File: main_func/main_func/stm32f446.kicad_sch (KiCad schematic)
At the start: 14 parts, among them J10 Conn_01x01_Male, J9 Conn_01x06_Male, SW2 SW_Push, U7 STM32F446RETx, Y1 8MHz

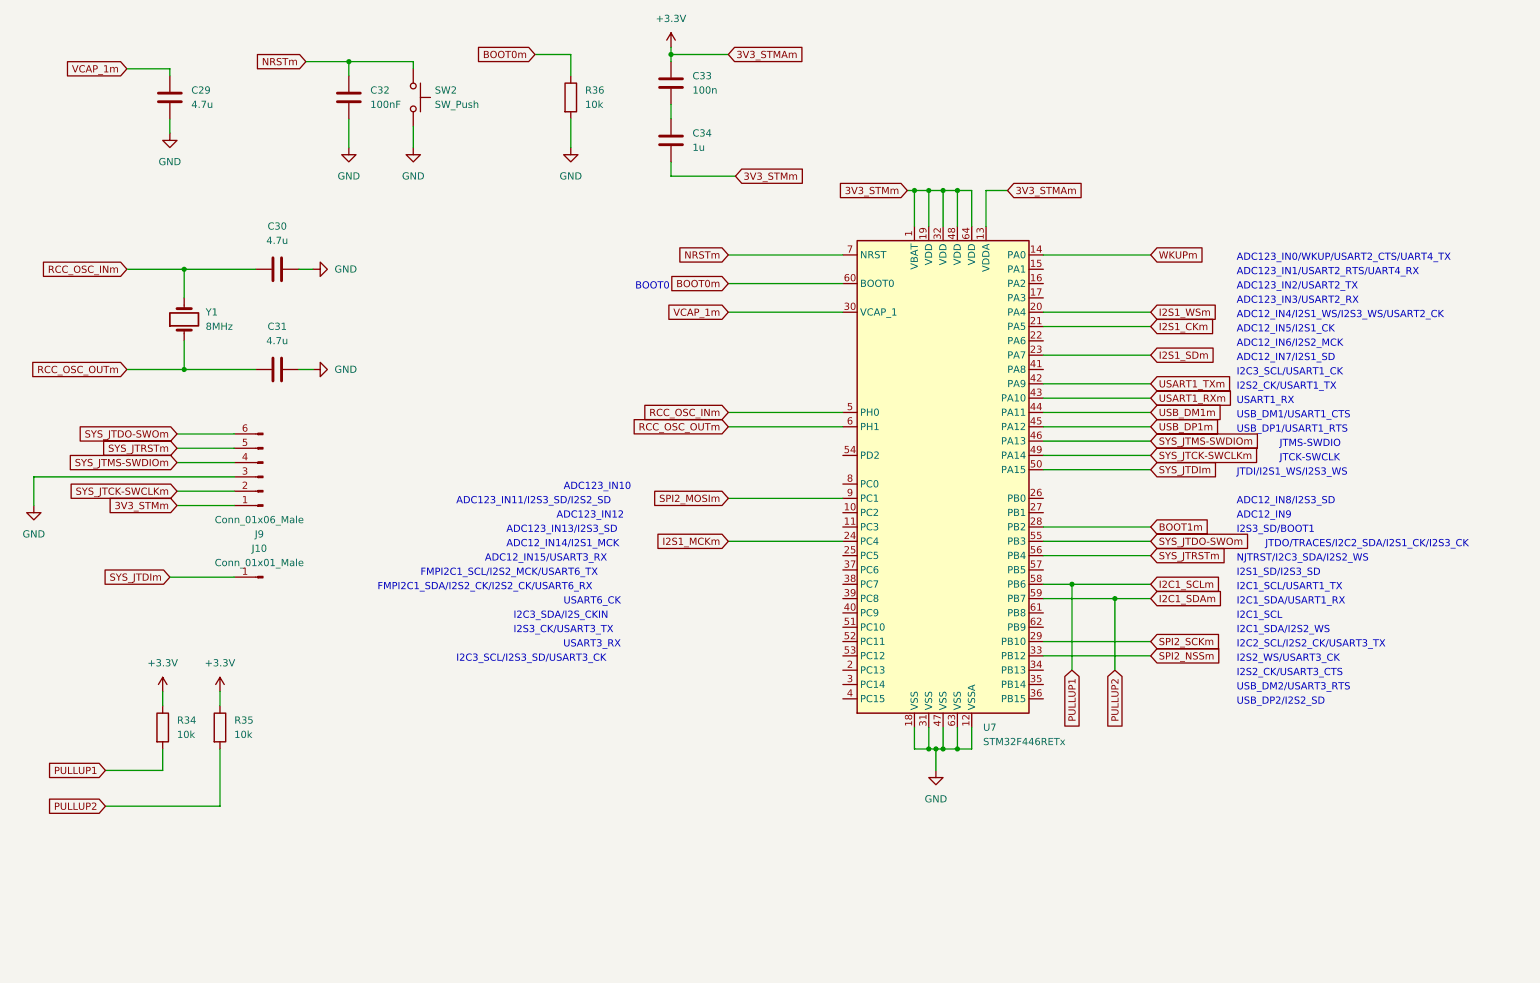
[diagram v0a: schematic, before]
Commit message: main func schematics fixed
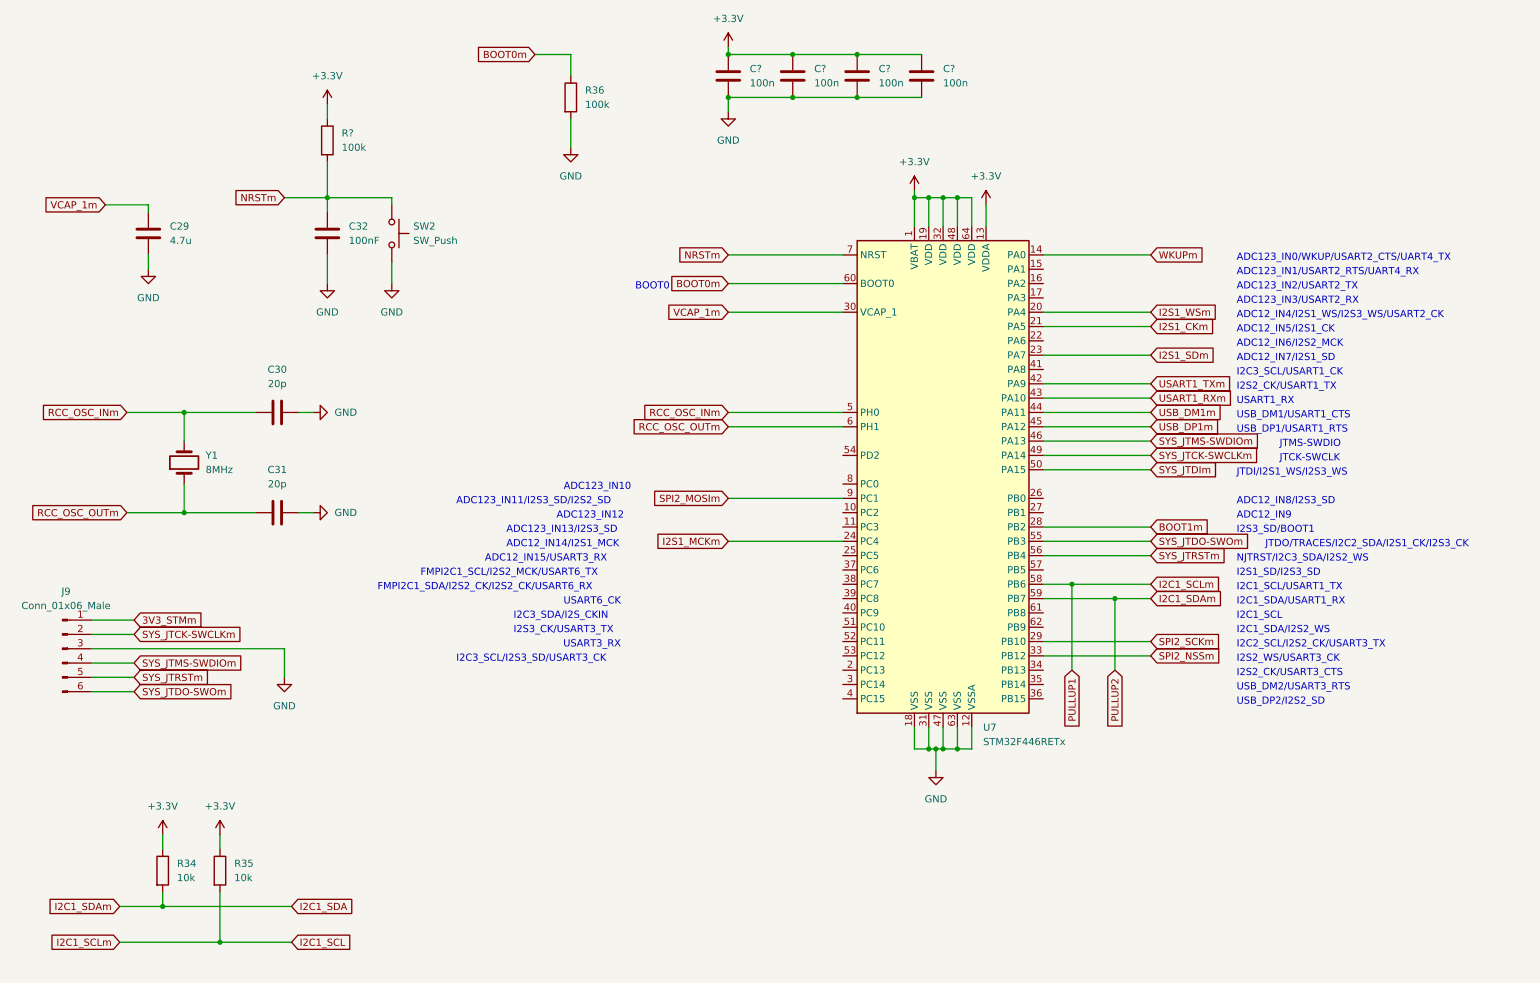
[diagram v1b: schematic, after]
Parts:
- removed C33: 100n, Capacitor_SMD:C_0805_2012Metric_Pad1.18x1.45mm_HandSolder, symbol Device:C
- removed C34: 1u, Capacitor_SMD:C_0805_2012Metric_Pad1.18x1.45mm_HandSolder, symbol Device:C
- removed J10: Conn_01x01_Male, Connector_PinSocket_2.54mm:PinSocket_1x01_P2.54mm_Horizontal, symbol Connector:Conn_01x01_Male
- added C? (x4): 100n, Capacitor_SMD:C_0805_2012Metric_Pad1.18x1.45mm_HandSolder, symbol Device:C
- added R?: 100k, Resistor_SMD:R_0805_2012Metric_Pad1.20x1.40mm_HandSolder, symbol Device:R
- C30, C31: value 4.7u -> 20p
- R36: value 10k -> 100k
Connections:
- net +3V3: now also U7.1 (VBAT), U7.19 (VDD), U7.32 (VDD), U7.48 (VDD), U7.64 (VDD), C?.1, C?.1, C?.1, C?.1, R?.1
- net 3V3_STMm: no longer U7.1 (VBAT), U7.19 (VDD), U7.32 (VDD), U7.48 (VDD), U7.64 (VDD)
- net GND: now also C?.2, C?.2, C?.2, C?.2
- net NRSTm: now also R?.2
- net I2C1_SCLm renamed I2C1_SCL
- net I2C1_SCL: now also R35.2; no longer R34.2
- net I2C1_SDAm renamed I2C1_SDA
- net I2C1_SDA: now also R34.2; no longer R35.2
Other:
- moved on the sheet: C29, C30, C31, C32, J9, R34, R35, SW2, Y1

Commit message: fixing keyboard and pot project schematics
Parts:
- gave numbers to parts that had none: 5
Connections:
- net 3V3_STMm is gone; now on net +3V3: J9.1 (Pin_1)
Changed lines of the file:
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@@
+    (stroke (width 0) (type default) (color 0 0 0 0))
+  )
+  (wire (pts (xy 31.75 124.46) (xy 41.91 124.46))
     (stroke (width 0) (type default) (color 0 0 0 0))
   )
@@
     (stroke (width 0) (type default) (color 0 0 0 0))
   )
+  (wire (pts (xy 41.91 124.46) (xy 41.91 123.19))
+    (stroke (width 0) (type default) (color 0 0 0 0))
+  )
   (wire (pts (xy 116.84 35.56) (xy 116.84 40.64))
     (stroke (width 0) (type default) (color 0 0 0 0))
@@
   )
   (wire (pts (xy 200.66 107.95) (xy 219.71 107.95))
-    (stroke (width 0) (type default) (color 0 0 0 0))
-  )
-  (wire (pts (xy 31.75 124.46) (xy 39.37 124.46))
     (stroke (width 0) (type default) (color 0 0 0 0))
   )
@@
     (effects (font (size 1.27 1.27)) (justify left))
     (property "Intersheet References" "${INTERSHEET_REFS}" (id 0) (at 232.8274 128.1906 0)
-      (effects (font (size 1.27 1.27)) (justify left) hide)
-    )
-  )
-  (global_label "3V3_STMm" (shape input) (at 39.37 124.46 0) (fields_autoplaced)
-    (effects (font (size 1.27 1.27)) (justify left))
-    (property "Intersheet References" "${INTERSHEET_REFS}" (id 0) (at 51.5802 124.5394 0)
       (effects (font (size 1.27 1.27)) (justify left) hide)
     )
@@
   (symbol (lib_id "power:+3.3V") (at 190.5 50.8 0) (unit 1)
     (in_bom yes) (on_board yes) (fields_autoplaced)
-    (property "Reference" "#PWR?" (id 0) (at 190.5 54.61 0)
+    (property "Reference" "#PWR054" (id 0) (at 190.5 54.61 0)
       (effects (font (size 1.27 1.27)) hide)
     )
@@
   (symbol (lib_id "power:+3.3V") (at 177.8 48.26 0) (unit 1)
     (in_bom yes) (on_board yes) (fields_autoplaced)
-    (property "Reference" "#PWR?" (id 0) (at 177.8 52.07 0)
+    (property "Reference" "#PWR053" (id 0) (at 177.8 52.07 0)
       (effects (font (size 1.27 1.27)) hide)
     )
@@
   (symbol (lib_id "Device:C") (at 179.07 27.94 0) (unit 1)
     (in_bom yes) (on_board yes) (fields_autoplaced)
-    (property "Reference" "C?" (id 0) (at 182.88 26.6699 0)
+    (property "Reference" "C36" (id 0) (at 182.88 26.6699 0)
       (effects (font (size 1.27 1.27)) (justify left))
     )
@@
   (symbol (lib_id "power:+3.3V") (at 73.66 33.02 0) (unit 1)
     (in_bom yes) (on_board yes) (fields_autoplaced)
-    (property "Reference" "#PWR?" (id 0) (at 73.66 36.83 0)
+    (property "Reference" "#PWR049" (id 0) (at 73.66 36.83 0)
       (effects (font (size 1.27 1.27)) hide)
     )
@@
   (symbol (lib_id "Device:C") (at 144.78 27.94 0) (unit 1)
     (in_bom yes) (on_board yes) (fields_autoplaced)
-    (property "Reference" "C?" (id 0) (at 148.59 26.6699 0)
+    (property "Reference" "C33" (id 0) (at 148.59 26.6699 0)
       (effects (font (size 1.27 1.27)) (justify left))
     )
@@
   (symbol (lib_id "Device:R") (at 73.66 39.37 0) (unit 1)
     (in_bom yes) (on_board yes) (fields_autoplaced)
-    (property "Reference" "R?" (id 0) (at 76.2 38.0999 0)
+    (property "Reference" "R40" (id 0) (at 76.2 38.0999 0)
       (effects (font (size 1.27 1.27)) (justify left))
     )
@@
   (symbol (lib_id "power:GND") (at 144.78 34.29 0) (unit 1)
     (in_bom yes) (on_board yes) (fields_autoplaced)
-    (property "Reference" "#PWR?" (id 0) (at 144.78 40.64 0)
+    (property "Reference" "#PWR052" (id 0) (at 144.78 40.64 0)
       (effects (font (size 1.27 1.27)) hide)
     )
@@
   (symbol (lib_id "Device:C") (at 167.64 27.94 0) (unit 1)
     (in_bom yes) (on_board yes) (fields_autoplaced)
-    (property "Reference" "C?" (id 0) (at 171.45 26.6699 0)
+    (property "Reference" "C35" (id 0) (at 171.45 26.6699 0)
       (effects (font (size 1.27 1.27)) (justify left))
     )
@@
   (symbol (lib_id "Device:C") (at 156.21 27.94 0) (unit 1)
     (in_bom yes) (on_board yes) (fields_autoplaced)
-    (property "Reference" "C?" (id 0) (at 160.02 26.6699 0)
+    (property "Reference" "C34" (id 0) (at 160.02 26.6699 0)
       (effects (font (size 1.27 1.27)) (justify left))
     )
@@
   (symbol (lib_id "power:+3.3V") (at 144.78 22.86 0) (unit 1)
     (in_bom yes) (on_board yes) (fields_autoplaced)
-    (property "Reference" "#PWR?" (id 0) (at 144.78 26.67 0)
+    (property "Reference" "#PWR050" (id 0) (at 144.78 26.67 0)
       (effects (font (size 1.27 1.27)) hide)
     )
@@
       (effects (font (size 1.27 1.27)) hide)
     )
+    (pin "1")
+  )
+  (symbol (lib_id "power:+3.3V") (at 41.91 123.19 0) (unit 1)
+    (in_bom yes) (on_board yes) (fields_autoplaced)
+    (property "Reference" "#PWR048" (id 0) (at 41.91 127 0)
+      (effects (font (size 1.27 1.27)) hide)
+    )
+    (property "Value" "+3.3V" (id 1) (at 41.91 118.11 0))
+    (property "Footprint" "" (id 2) (at 41.91 123.19 0)
+      (effects (font (size 1.27 1.27)) hide)
+    )
+    (property "Datasheet" "" (id 3) (at 41.91 123.19 0)
+      (effects (font (size 1.27 1.27)) hide)
+    )

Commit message: main_func pcb done
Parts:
- added D8: GREEN LED, LED_SMD:LED_0805_2012Metric_Pad1.15x1.40mm_HandSolder, symbol Device:LED
- added D9: RED LED, LED_SMD:LED_0805_2012Metric_Pad1.15x1.40mm_HandSolder, symbol Device:LED
- added R41, R42: 1k, Resistor_SMD:R_0805_2012Metric_Pad1.20x1.40mm_HandSolder, symbol Device:R
- C32: value 100nF -> 100n
- SW2: footprint (none) -> tactile_button:ROCPU Switches TP10721645
- Y1: footprint Crystal:Crystal_SMD_3225-4Pin_3.2x2.5mm_HandSoldering -> Crystal:Crystal_SMD_HC49-SD_HandSoldering
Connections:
- net BOOT1m is gone; now on net GND: U7.28 (PB2)
- net +3V3: now also D8.2 (A)
- net GND: now also D9.1 (K)
- net USART3_RXm: now reaches U7.25 (PC5)
- net USART3_TXm: now reaches U7.51 (PC10)
- net USART3_TXm: now also R41.1, R42.1
- new net: D9.2 (A), R42.2
- new net: D8.1 (K), R41.2

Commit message: pcb design fixing
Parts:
- R40: value 100k -> 10k
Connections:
- net WKUPm: no longer names the net of U7.14 (PA0)
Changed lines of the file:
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@@
   (junction (at 132.08 148.59) (diameter 0) (color 0 0 0 0)
   )
-  (junction (at 213.36 120.65) (diameter 0) (color 0 0 0 0)
-  )
   (junction (at 48.26 105.41) (diameter 0) (color 0 0 0 0)
   )
@@
   (junction (at 180.34 147.32) (diameter 0) (color 0 0 0 0)
   )
-  (junction (at 205.74 118.11) (diameter 0) (color 0 0 0 0)
-  )
   (junction (at 182.88 49.53) (diameter 0) (color 0 0 0 0)
   )
@@
     (stroke (width 0) (type default) (color 0 0 0 0))
   )
-  (wire (pts (xy 213.36 120.65) (xy 219.71 120.65))
-    (stroke (width 0) (type default) (color 0 0 0 0))
-  )
-  (wire (pts (xy 205.74 118.11) (xy 205.74 133.35))
-    (stroke (width 0) (type default) (color 0 0 0 0))
-  )
   (wire (pts (xy 177.8 147.32) (xy 177.8 143.51))
     (stroke (width 0) (type default) (color 0 0 0 0))
@@
     (stroke (width 0) (type default) (color 0 0 0 0))
   )
-  (wire (pts (xy 200.66 118.11) (xy 205.74 118.11))
-    (stroke (width 0) (type default) (color 0 0 0 0))
-  )
   (wire (pts (xy 200.66 107.95) (xy 227.33 107.95))
     (stroke (width 0) (type default) (color 0 0 0 0))
@@
     (stroke (width 0) (type default) (color 0 0 0 0))
   )
-  (wire (pts (xy 200.66 120.65) (xy 213.36 120.65))
+  (wire (pts (xy 200.66 120.65) (xy 219.71 120.65))
     (stroke (width 0) (type default) (color 0 0 0 0))
   )
@@
     (stroke (width 0) (type default) (color 0 0 0 0))
   )
-  (wire (pts (xy 213.36 120.65) (xy 213.36 133.35))
-    (stroke (width 0) (type default) (color 0 0 0 0))
-  )
   (wire (pts (xy 185.42 147.32) (xy 182.88 147.32))
     (stroke (width 0) (type default) (color 0 0 0 0))
@@
     (stroke (width 0) (type default) (color 0 0 0 0))
   )
-  (wire (pts (xy 200.66 59.69) (xy 219.71 59.69))
-    (stroke (width 0) (type default) (color 0 0 0 0))
-  )
   (wire (pts (xy 200.66 92.71) (xy 219.71 92.71))
     (stroke (width 0) (type default) (color 0 0 0 0))
@@
     (stroke (width 0) (type default) (color 0 0 0 0))
   )
-  (wire (pts (xy 205.74 118.11) (xy 219.71 118.11))
+  (wire (pts (xy 200.66 118.11) (xy 219.71 118.11))
     (stroke (width 0) (type default) (color 0 0 0 0))
   )
@@
     )
   )
-  (global_label "WKUPm" (shape input) (at 219.71 59.69 0) (fields_autoplaced)
-    (effects (font (size 1.27 1.27)) (justify left))
-    (property "Intersheet References" "${INTERSHEET_REFS}" (id 0) (at 229.1383 59.6106 0)
-      (effects (font (size 1.27 1.27)) (justify left) hide)
-    )
-  )
   (global_label "I2C1_SCLm" (shape input) (at 219.71 118.11 0) (fields_autoplaced)
     (effects (font (size 1.27 1.27)) (justify left))
@@
     )
   )
-  (global_label "PULLUP1" (shape input) (at 205.74 133.35 270) (fields_autoplaced)
-    (effects (font (size 1.27 1.27)) (justify right))
-    (property "Intersheet References" "${INTERSHEET_REFS}" (id 0) (at 205.6606 144.2298 90)
-      (effects (font (size 1.27 1.27)) (justify right) hide)
-    )
-  )
   (global_label "I2C1_SDA" (shape input) (at 67.31 175.26 0) (fields_autoplaced)
     (effects (font (size 1.27 1.27)) (justify left))
@@
     (property "Intersheet References" "${INTERSHEET_REFS}" (id 0) (at 60.2283 126.9206 0)
       (effects (font (size 1.27 1.27)) (justify left) hide)
-    )
-  )
-  (global_label "PULLUP2" (shape input) (at 213.36 133.35 270) (fields_autoplaced)
-    (effects (font (size 1.27 1.27)) (justify right))
-    (property "Intersheet References" "${INTERSHEET_REFS}" (id 0) (at 213.2806 144.2298 90)
-      (effects (font (size 1.27 1.27)) (justify right) hide)
     )
   )
@@
       (effects (font (size 1.27 1.27)) (justify left))
     )
-    (property "Value" "100k" (id 1) (at 76.2 40.6399 0)
-      (effects (font (size 1.27 1.27)) (justify left))
-    )
+    (property "Value" "10k" (id 1) (at 76.2 40.6399 0)
+      (effects (font (size 1.27 1.27)) (justify left))
+    )
